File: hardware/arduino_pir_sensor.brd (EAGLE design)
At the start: 69 x 34.8 mm, 44 parts, among them U2 TPS61097-33, U3 BISS0001SO16, U4 NRF24L01+_MODULE, U5 D203S

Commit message: - schematic pdf file updated
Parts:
- JP1: value (none) -> Serial
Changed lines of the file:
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@@
 <attribute name="MF" value="" x="25.908" y="18.542" size="0.8128" layer="27" ratio="10" rot="R270" display="off"/>
 </element>
-<element name="JP1" library="endy-connectors" package="1X03" value="" x="66.548" y="7.112" smashed="yes" rot="R270">
+<element name="JP1" library="endy-connectors" package="1X03" value="Serial" x="66.548" y="7.112" smashed="yes" rot="R270">
 <attribute name="NAME" x="62.1538" y="0.3048" size="1.27" layer="51" ratio="10"/>
 <attribute name="VALUE" x="63.373" y="8.382" size="1.27" layer="27" rot="R270"/>
@@
 </signal>
 </signals>
-<errors>
-</errors>
 </board>
 </drawing>

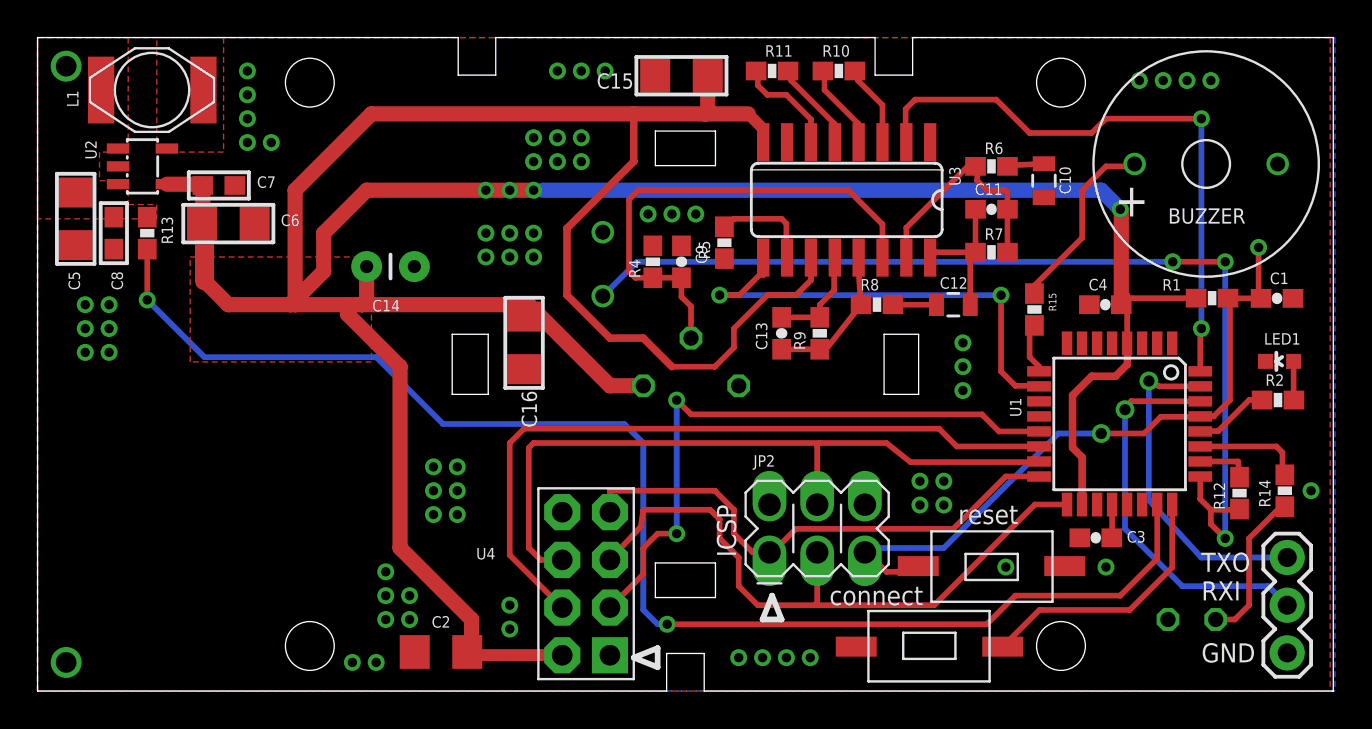
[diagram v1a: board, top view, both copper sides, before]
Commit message: - extra power line capacitor added - "connect" button moved away from the mounting screw
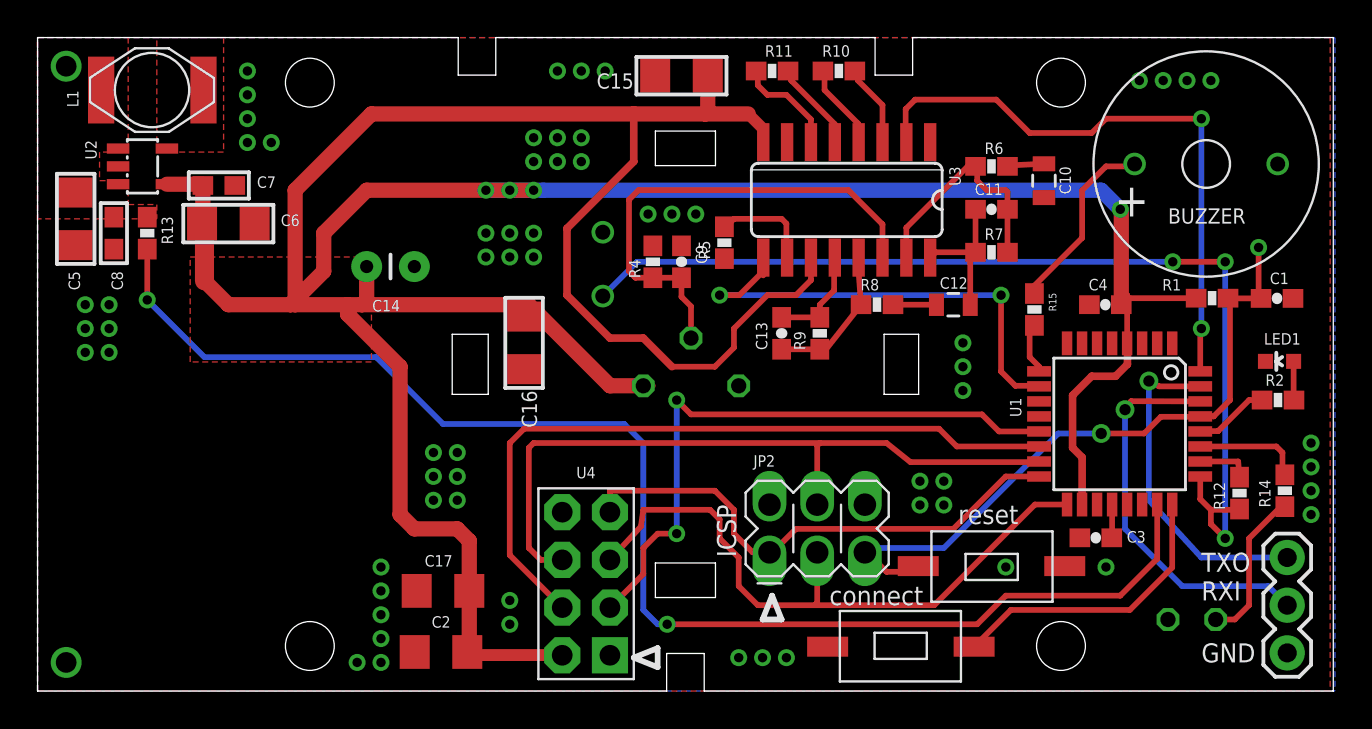
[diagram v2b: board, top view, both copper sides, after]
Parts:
- added C17: 10uF, SparkFun-Capacitors:1206
- moved S2 1.52 mm to (46.0, 2.41)
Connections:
- net 3.3V: now also C17.1
- net GND: now also C17.2
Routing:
- net 3.3V: track 206.3 -> 207.8 mm
- net A1: track 14.1 -> 15.7 mm

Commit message: change value of the photo cell divider resistor to 47K from 510K
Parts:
- R12: value 510K -> 47K
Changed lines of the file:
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@@
 <attribute name="VALUE" x="40.132" y="34.163" size="0.4064" layer="27" font="vector" rot="R180"/>
 </element>
-<element name="R12" library="SparkFun-Resistors" package="0603-RES" value="510K" x="64.008" y="10.541" smashed="yes" rot="R90">
+<element name="R12" library="SparkFun-Resistors" package="0603-RES" value="47K" x="64.008" y="10.541" smashed="yes" rot="R90">
 <attribute name="OC_NEWARK" value="unknown" x="64.008" y="10.541" size="1.778" layer="27" rot="R90" display="off"/>
 <attribute name="MF" value="" x="64.008" y="10.541" size="1.778" layer="27" rot="R90" display="off"/>

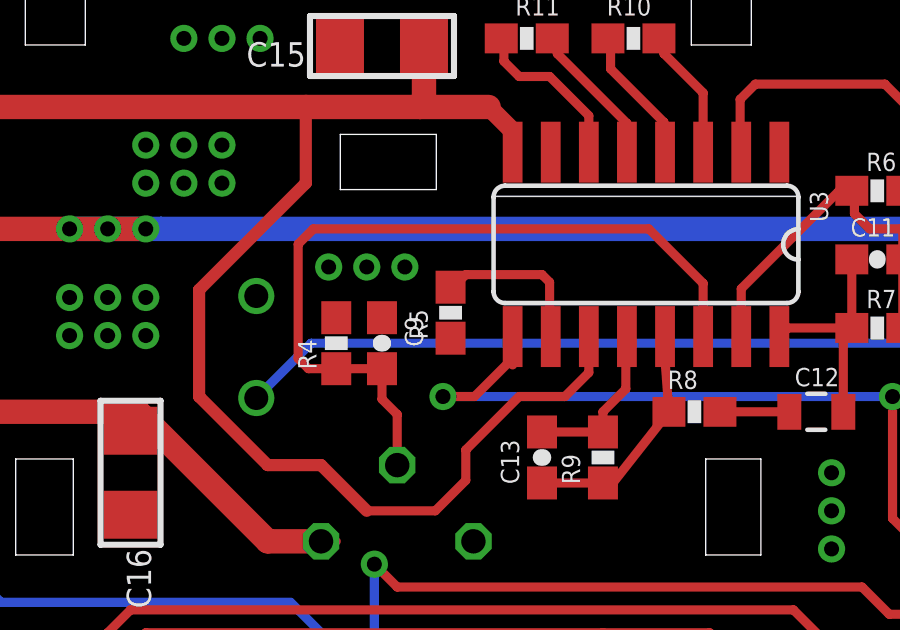
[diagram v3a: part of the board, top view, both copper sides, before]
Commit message: - resistor values fixed
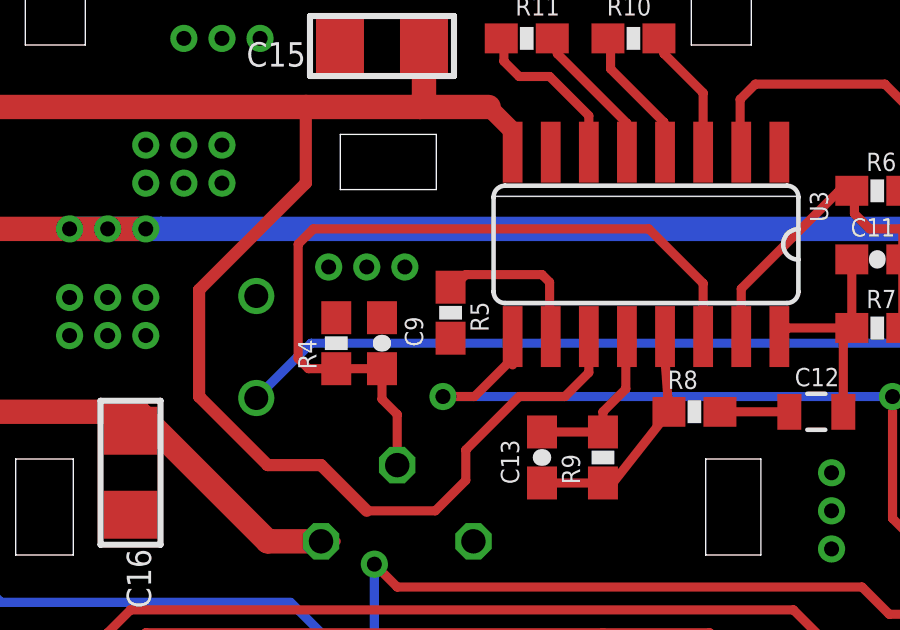
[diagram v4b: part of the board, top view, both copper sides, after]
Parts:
- R13: value 2M -> 680K
- R15: value 2M -> 100
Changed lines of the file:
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@@
 <attribute name="MF" value="" x="36.576" y="23.876" size="1.778" layer="27" rot="R90" display="off"/>
 <attribute name="MPN" value="" x="36.576" y="23.876" size="1.778" layer="27" rot="R90" display="off"/>
-<attribute name="NAME" x="35.814" y="22.987" size="0.6096" layer="25" font="vector" ratio="10" rot="R90"/>
+<attribute name="NAME" x="37.846" y="23.241" size="0.6096" layer="25" font="vector" ratio="10" rot="R90"/>
 <attribute name="VALUE" x="37.719" y="22.86" size="0.4064" layer="27" font="vector" rot="R90"/>
 </element>
@@
 <attribute name="VALUE" x="65.151" y="9.525" size="0.4064" layer="27" font="vector" rot="R90"/>
 </element>
-<element name="R13" library="SparkFun-Resistors" package="0603-RES" value="2M" x="5.842" y="24.384" smashed="yes" rot="R270">
+<element name="R13" library="SparkFun-Resistors" package="0603-RES" value="680K" x="5.842" y="24.384" smashed="yes" rot="R270">
 <attribute name="OC_NEWARK" value="unknown" x="5.842" y="24.384" size="1.778" layer="27" rot="R270" display="off"/>
 <attribute name="MF" value="" x="5.842" y="24.384" size="1.778" layer="27" rot="R270" display="off"/>
@@
 <attribute name="NAME" x="29.718" y="11.938" size="0.6096" layer="25" rot="R180"/>
 </element>
-<element name="R15" library="SparkFun-Resistors" package="0603-RES" value="2M" x="53.086" y="20.32" rot="R270">
+<element name="R15" library="SparkFun-Resistors" package="0603-RES" value="100" x="53.086" y="20.32" rot="R270">
 <attribute name="OC_NEWARK" value="unknown" x="53.086" y="20.32" size="0.8128" layer="27" ratio="10" rot="R270" display="off"/>
 <attribute name="MPN" value="" x="53.086" y="20.32" size="0.8128" layer="27" ratio="10" rot="R270" display="off"/>

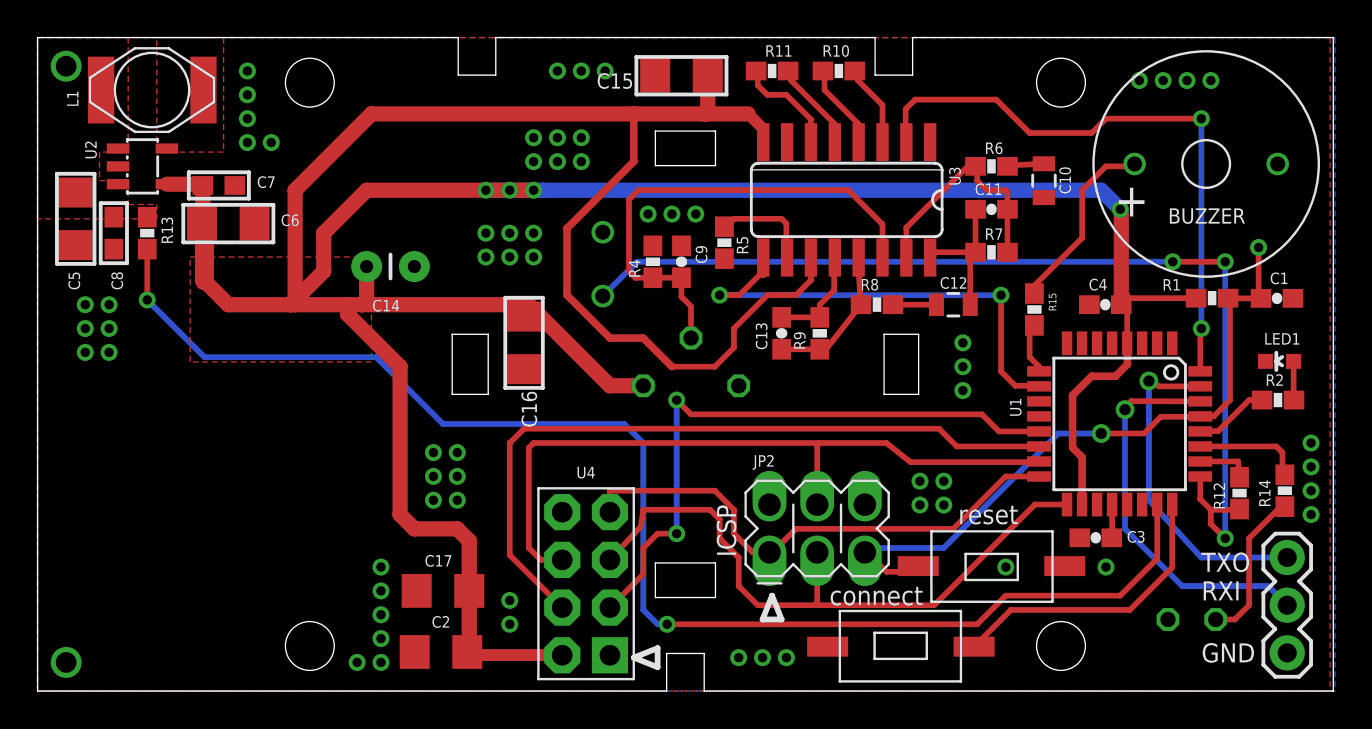
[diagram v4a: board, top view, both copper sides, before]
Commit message: - minor reroute power lines for  BISS0001 - contact pads for external power supply added
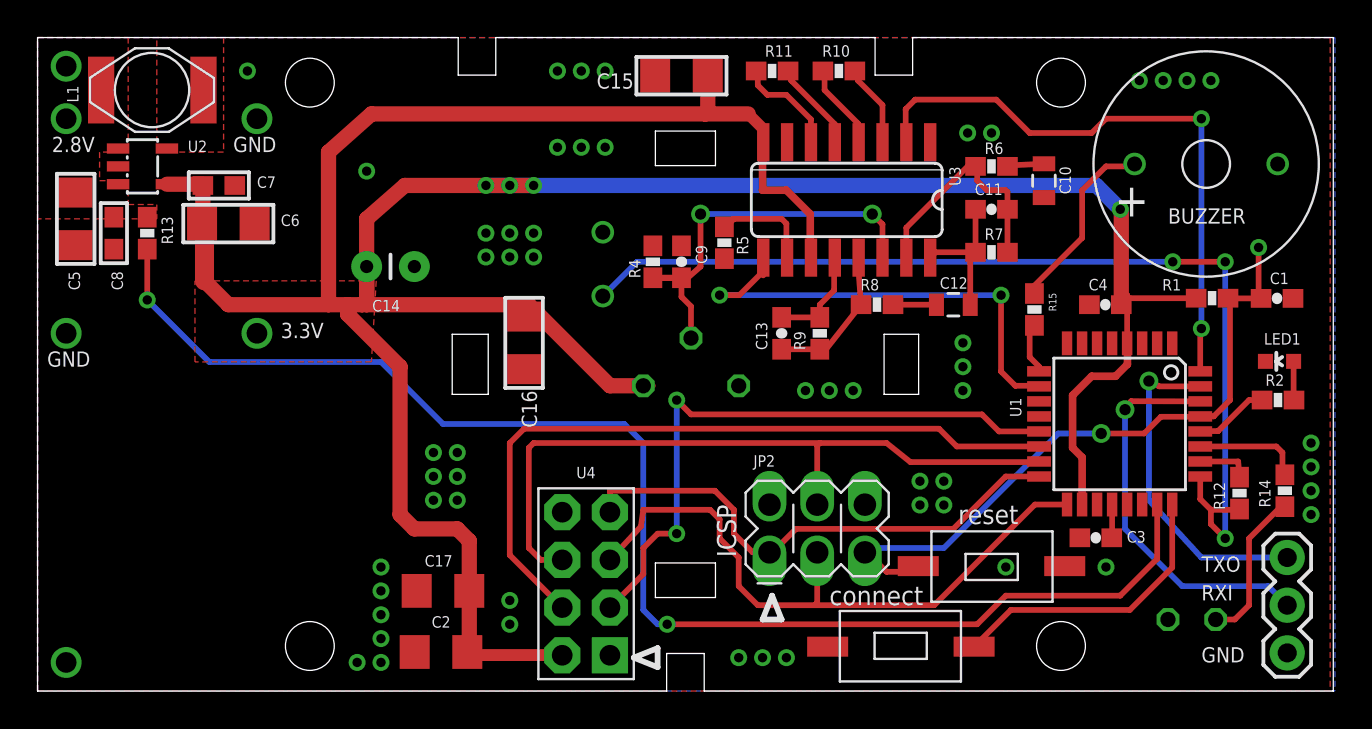
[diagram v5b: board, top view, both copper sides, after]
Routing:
- net 3.3V: track 207.8 -> 183.3 mm, vias 4 -> 5
- net N$2: track 26.4 -> 22.2 mm, vias 0 -> 2
- net 2.8V: vias 1 -> 2
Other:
- board text added: "2.8V"
- board text added: "3.3V"
- board text added: "PIR sensor rev 1.2"
- board text removed: "PIR sensor rev 1.1"
